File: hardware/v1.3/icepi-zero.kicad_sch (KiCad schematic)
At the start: 29 parts, among them J1 Conn_02x20_Counter_Clockwise, SW1 SW_Push, SW2 SW_Push, U1 ECP5-CABGA256, Y1 SG-8018CG 50.000000MHz

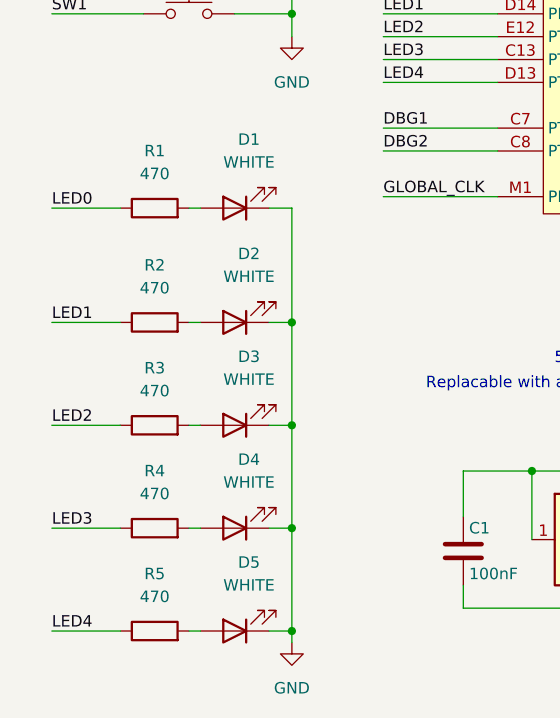
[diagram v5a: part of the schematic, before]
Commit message: Change LED's resistor values to make them dimmer
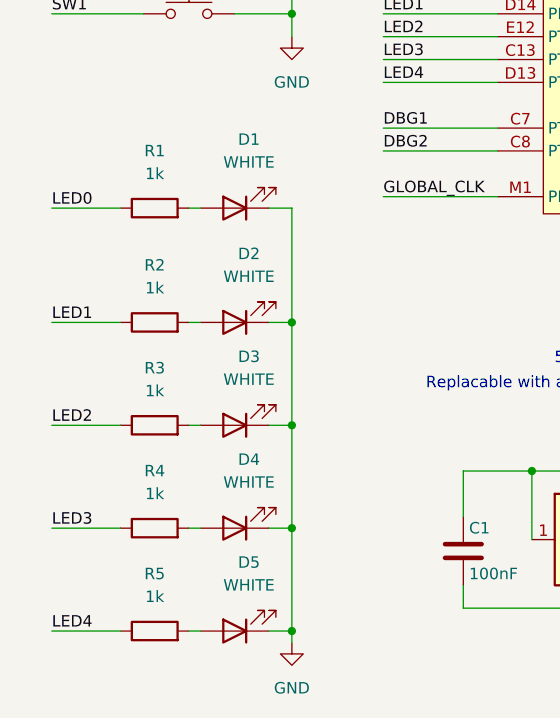
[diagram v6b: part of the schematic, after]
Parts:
- R1, R2, R3, R4, R5: value 470 -> 1k; LCSC Link https://lcsc.com/product-detail/Chip-Resistor-Surface-Mount_UNI-ROYAL-0402WGF4700TCE_C25117.html -> https://lcsc.com/product-detail/Chip-Resistor-Surface-Mount_UNI-ROYAL-0402WGF1001TCE_C11702.html; LCSC Part # C25117 -> C11702; Manufactuer Part Number 0402WGF4700TCE -> 0402WGF1001TCE
